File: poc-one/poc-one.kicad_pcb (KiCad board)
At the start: 2 copper layers, 275 x 200 mm, 81 parts, among them J4 Connector, USB-TYPE-C-16P, Q1 SS8550 Y2 200-350, Q2 SS8550 Y2 200-350, Q3 SS8550 Y2 200-350, Q5 SS8550 Y2 200-350, SW1 SW_Push, SW2 SW_Push, U1 RP2350_80QFN, U11 74HC595D, U13 74HC595D, U2 NCP1117-3.3_SOT223, U3 W25Q128, U4 74HC138, U9 74HC595D, Y1 ABM8-272-T3

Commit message: schematic-v2
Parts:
- added REF**: B2B Pad, TFPC:B2B Pad, F.Cu at (184.0, 81.1)
- added REF**: B2B Pad, TFPC:B2B Pad, F.Cu at (152.4, 80.5)
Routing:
- net /LED_control/LED_matrix/G2: track 14.4 -> 13.8 mm
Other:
- board outline removed

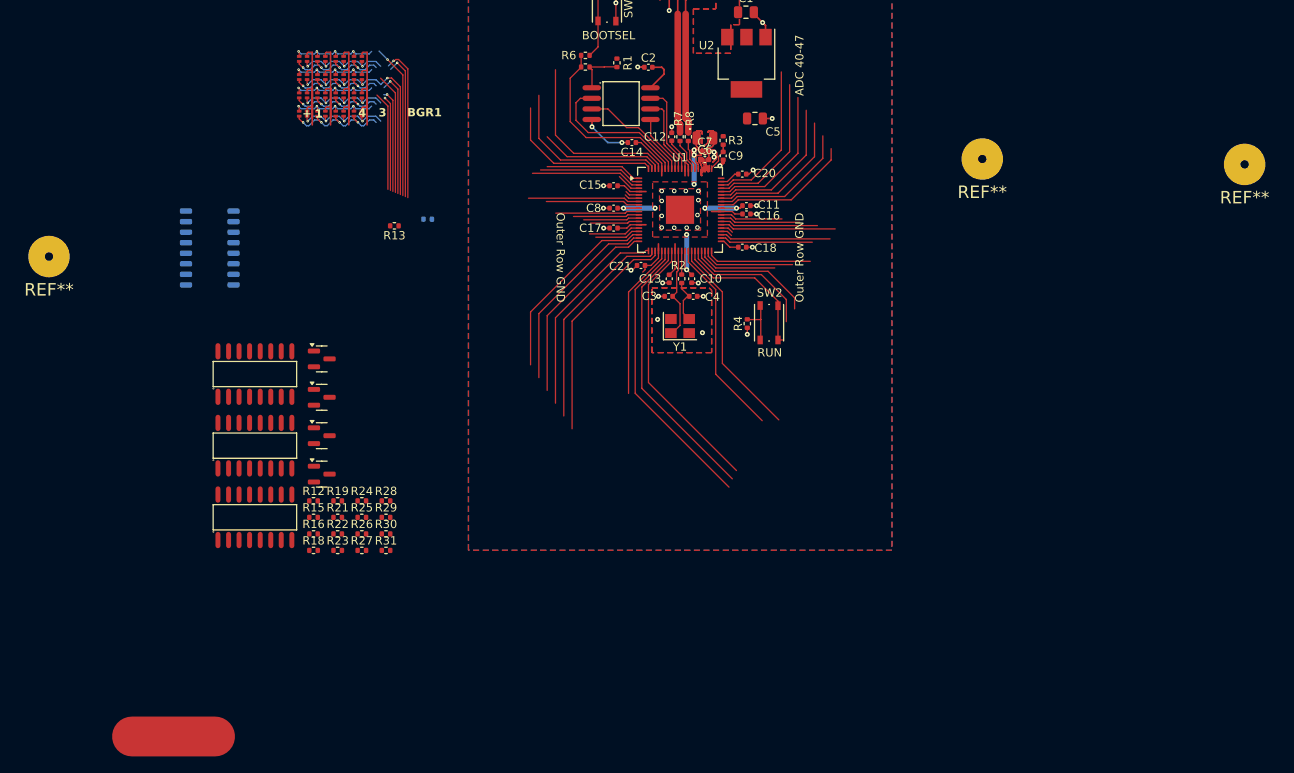
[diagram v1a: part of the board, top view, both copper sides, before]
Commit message: fixed a couple resistors, reworked footprints incl. datasheets
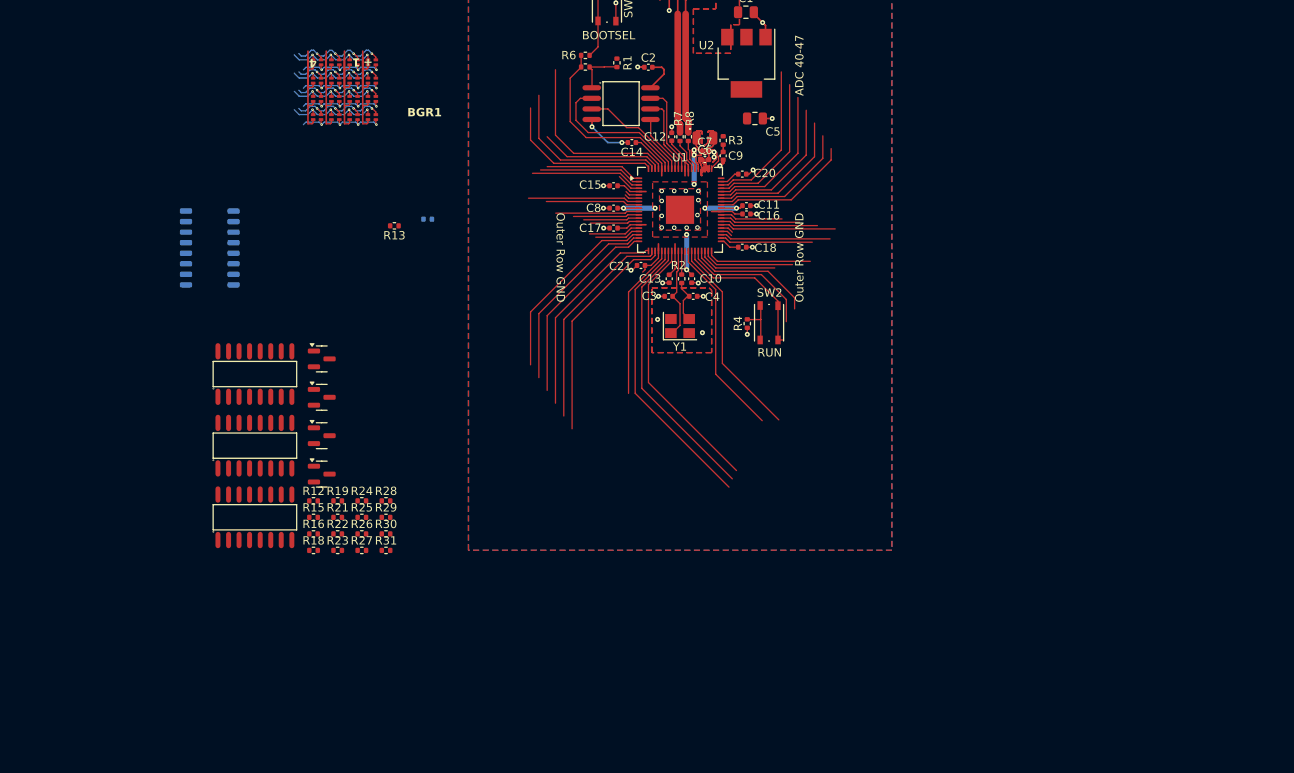
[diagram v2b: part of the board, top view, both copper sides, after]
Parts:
- removed REF** (x3): B2B Pad, TFPC:B2B Pad
- moved D1 10.9 mm to (78.9, 75.4)
- moved D13 10.3 mm to (78.9, 68.8), turned to 180 degrees
- moved D5 8.68 mm to (78.9, 73.2), turned to 180 degrees
- moved D4 8.57 mm to (72.3, 75.4), turned to 180 degrees
- moved D9 8.47 mm to (78.9, 71.0), turned to 180 degrees
- moved D2 8.02 mm to (76.7, 75.4)
- moved D16 7.90 mm to (72.3, 68.8), turned to 180 degrees
- moved D14 7.30 mm to (76.7, 68.8), turned to 180 degrees
- moved D3 7.04 mm to (74.5, 75.4), turned to 180 degrees
- moved D15 6.20 mm to (74.5, 68.8), turned to 180 degrees
- moved D8 5.57 mm to (72.3, 73.2), turned to 180 degrees
- moved D12 5.23 mm to (72.3, 71.0), turned to 180 degrees
- moved D6 4.68 mm to (76.7, 73.2), turned to 180 degrees
- moved D10 4.27 mm to (76.7, 71.0), turned to 180 degrees
- moved D7 2.67 mm to (74.5, 73.2), turned to 180 degrees
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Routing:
- net /LED_control/LED_matrix/R1: track 52.5 -> 12.7 mm, vias 7 -> 4
- net /LED_control/LED_matrix/R0: track 31.3 -> 12.7 mm, vias 5 -> 4
- net /LED_control/LED_matrix/B0: track 30.3 -> 11.7 mm, vias 5 -> 4
- net /LED_control/LED_matrix/G0: track 31.5 -> 13.8 mm, vias 5 -> 4
- net /LED_control/LED_matrix/G1: track 28.8 -> 13.8 mm, vias 5 -> 4
- net /LED_control/LED_matrix/B1: track 26.2 -> 11.7 mm
- net /LED_control/LED_matrix/B2: track 23.6 -> 11.7 mm
- net (no net): track 10.0 -> 0.00 mm
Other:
- board text removed: "3"

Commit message: poc-one routed & schematic changes
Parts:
- removed C3: 15p, Capacitor_SMD:C_0402_1005Metric
- removed the R13 at (81.6, 88.5)
- removed the R13 at (85.6, 87.7)
- removed R2: 1k, Resistor_SMD:R_0402_1005Metric
- removed U1: RP2350_80QFN, Package_DFN_QFN:QFN-80-1EP_10x10mm_P0.4mm_EP3.4x3.4mm
- removed U11, U13, U9: 74HC595D, PCM_JLCPCB:SOIC-16_L9.9-W3.9-P1.27-LS6.0-BL
- added BT1: Battery_Cell, TFPC:BH-18650-B6AA002, F.Cu at (148.4, 167.6)
- added C19: 1u, Capacitor_SMD:C_0402_1005Metric, F.Cu at (117.3, 119.7)
- added C22: 4.7u, Capacitor_SMD:C_0402_1005Metric, F.Cu at (119.6, 117.2)
- added C23: 10u, Capacitor_SMD:C_0402_1005Metric, F.Cu at (124.7, 121.7)
- added C24: 10u, Capacitor_SMD:C_0402_1005Metric, F.Cu at (127.7, 121.7)
- added C25: 10u, Capacitor_SMD:C_0402_1005Metric, F.Cu at (146.9, 119.6)
- added C26: 10u, Capacitor_SMD:C_0402_1005Metric, F.Cu at (155.7, 114.7)
- added C27: 100u, Capacitor_SMD:CP_Elec_5x5.4, F.Cu at (91.2, 206.4)
- added C35: 10u, Capacitor_SMD:C_0402_1005Metric, F.Cu at (124.0, 129.7)
- added C36: 10u, Capacitor_SMD:C_0402_1005Metric, F.Cu at (126.0, 136.4)
- added C37: 100p, Capacitor_SMD:C_0402_1005Metric, F.Cu at (124.0, 130.8)
- added C38: 100n, Capacitor_SMD:C_0402_1005Metric, F.Cu at (124.3, 137.3)
- added C39: 100n, Capacitor_SMD:C_0402_1005Metric, F.Cu at (114.3, 136.2)
- added D17: LED_RABG, TFPC:NH-B1212RGBA-HF, F.Cu at (99.7, 193.2)
- added D18: LED_RABG, TFPC:NH-B1212RGBA-HF, F.Cu at (101.9, 193.2)
- added D19: LED_RABG, TFPC:NH-B1212RGBA-HF, F.Cu at (104.1, 193.2)
- added J1: MASTER_FANOUT, Connector_PinHeader_2.54mm:PinHeader_2x10_P2.54mm_Vertical, F.Cu at (103.2, 114.1)
- added J2: SUBG_FANOUT, Connector_PinHeader_2.54mm:PinHeader_2x10_P2.54mm_Vertical, F.Cu at (83.6, 130.8)
- added J3: Connector, USB-TYPE-C-16P, PCM_JLCPCB:TYPE-C-SMD_HX-TYPE-C-16PIN, F.Cu at (110.3, 112.7)
- added J5: DEBUG, Connector_PinHeader_2.54mm:PinHeader_1x03_P2.54mm_Vertical, F.Cu at (112.8, 151.3)
- added JP1: SolderJumper_2_Bridged, Jumper:SolderJumper-2_P1.3mm_Bridged_Pad1.0x1.5mm, F.Cu at (93.8, 162.6)
- added JP10: SolderJumper_2_Bridged, Jumper:SolderJumper-2_P1.3mm_Bridged_Pad1.0x1.5mm, F.Cu at (107.2, 166.3)
- added JP11: SolderJumper_2_Bridged, Jumper:SolderJumper-2_P1.3mm_Bridged_Pad1.0x1.5mm, F.Cu at (108.4, 162.6)
- added JP12: SolderJumper_2_Bridged, Jumper:SolderJumper-2_P1.3mm_Bridged_Pad1.0x1.5mm, F.Cu at (109.8, 166.3)
- added JP13: SolderJumper_2_Bridged, Jumper:SolderJumper-2_P1.3mm_Bridged_Pad1.0x1.5mm, F.Cu at (110.9, 162.6)
- added JP14: SolderJumper_2_Bridged, Jumper:SolderJumper-2_P1.3mm_Bridged_Pad1.0x1.5mm, F.Cu at (113.0, 166.3)
- added JP15: SolderJumper_2_Bridged, Jumper:SolderJumper-2_P1.3mm_Bridged_Pad1.0x1.5mm, F.Cu at (114.1, 162.6)
- added JP16: SolderJumper_2_Bridged, Jumper:SolderJumper-2_P1.3mm_Bridged_Pad1.0x1.5mm, F.Cu at (115.5, 166.3)
- added JP17: SolderJumper_2_Bridged, Jumper:SolderJumper-2_P1.3mm_Bridged_Pad1.0x1.5mm, F.Cu at (116.7, 162.6)
- added JP18: SolderJumper_2_Bridged, Jumper:SolderJumper-2_P1.3mm_Bridged_Pad1.0x1.5mm, F.Cu at (118.9, 166.3)
- added JP19: SolderJumper_2_Bridged, Jumper:SolderJumper-2_P1.3mm_Bridged_Pad1.0x1.5mm, F.Cu at (120.0, 162.6)
- added JP2: SolderJumper_2_Bridged, Jumper:SolderJumper-2_P1.3mm_Bridged_Pad1.0x1.5mm, F.Cu at (95.2, 166.3)
- added JP20: SolderJumper_2_Bridged, Jumper:SolderJumper-2_P1.3mm_Bridged_Pad1.0x1.5mm, F.Cu at (121.5, 166.3)
- added JP21: SolderJumper_2_Bridged, Jumper:SolderJumper-2_P1.3mm_Bridged_Pad1.0x1.5mm, F.Cu at (122.6, 162.6)
- added JP3: SolderJumper_2_Bridged, Jumper:SolderJumper-2_P1.3mm_Bridged_Pad1.0x1.5mm, F.Cu at (96.3, 162.6)
- added JP4: SolderJumper_2_Bridged, Jumper:SolderJumper-2_P1.3mm_Bridged_Pad1.0x1.5mm, F.Cu at (98.8, 166.2)
- added JP5: SolderJumper_2_Bridged, Jumper:SolderJumper-2_P1.3mm_Bridged_Pad1.0x1.5mm, F.Cu at (99.9, 162.6)
- added JP6: SolderJumper_2_Bridged, Jumper:SolderJumper-2_P1.3mm_Bridged_Pad1.0x1.5mm, F.Cu at (101.3, 166.2)
- added JP7: SolderJumper_2_Bridged, Jumper:SolderJumper-2_P1.3mm_Bridged_Pad1.0x1.5mm, F.Cu at (102.5, 162.6)
- added JP8: SolderJumper_2_Bridged, Jumper:SolderJumper-2_P1.3mm_Bridged_Pad1.0x1.5mm, F.Cu at (103.8, 166.2)
- added JP9: SolderJumper_2_Bridged, Jumper:SolderJumper-2_P1.3mm_Bridged_Pad1.0x1.5mm, F.Cu at (105.0, 162.6)
- added L2: 2u2, Inductor_SMD:L_0603_1608Metric, F.Cu at (126.3, 121.2)
- added MK1: LMA2718T421-OA5-2, TFPC:LMA2718T421-OA5-2, F.Cu at (121.3, 130.7)
- added Q4: SS8550 Y2 200-350, PCM_JLCPCB:Q_SOT-23, F.Cu at (101.2, 197.6)
- added Q6: SS8550 Y2 200-350, PCM_JLCPCB:Q_SOT-23, F.Cu at (110.5, 197.6)
- added Q7: XYC-PT0805BC-L4-D, PCM_JLCPCB:D_0805, F.Cu at (121.2, 141.2)
- added R11: 5.1k, Resistor_SMD:R_0402_1005Metric, F.Cu at (107.5, 118.7)
- added R13: 2.2k, Resistor_SMD:R_0402_1005Metric, F.Cu at (117.0, 122.9)
- added R14: 100m, Resistor_SMD:R_1206_3216Metric, F.Cu at (113.8, 119.8)
- added R17: 10k, Resistor_SMD:R_0402_1005Metric, F.Cu at (121.9, 128.2)
- added R20: 1.5k, Resistor_SMD:R_0402_1005Metric, F.Cu at (120.0, 128.2)
- added R32: 130, Resistor_SMD:R_0402_1005Metric, F.Cu at (92.1, 180.9)
- added R33: 360, Resistor_SMD:R_0402_1005Metric, F.Cu at (101.1, 180.8)
- added R34: 82, Resistor_SMD:R_0402_1005Metric, F.Cu at (113.5, 181.0)
- added R35: 130, Resistor_SMD:R_0402_1005Metric, F.Cu at (93.5, 180.9)
- added R36: 360, Resistor_SMD:R_0402_1005Metric, F.Cu at (102.2, 180.8)
- added R37: 82, Resistor_SMD:R_0402_1005Metric, F.Cu at (114.8, 181.0)
- added R38: 360, Resistor_SMD:R_0402_1005Metric, F.Cu at (103.4, 180.8)
- added R39: 82, Resistor_SMD:R_0402_1005Metric, F.Cu at (116.1, 181.0)
- added R40: 360, Resistor_SMD:R_0402_1005Metric, F.Cu at (104.6, 180.8)
- added R41: 2k, Resistor_SMD:R_0402_1005Metric, F.Cu at (125.7, 130.9)
- added R42: 10k, Resistor_SMD:R_0402_1005Metric, F.Cu at (118.8, 141.2)
- added R43: 10k, Resistor_SMD:R_0402_1005Metric, F.Cu at (127.2, 136.2)
- added R44: 10k, Resistor_SMD:R_0402_1005Metric, F.Cu at (124.3, 136.3)
- added R45: 100k, Resistor_SMD:R_0402_1005Metric, F.Cu at (124.0, 131.8)
- added R46: 100, Resistor_SMD:R_0402_1005Metric, F.Cu at (121.4, 134.3)
- added SW3: BAT_SYS_PWR HY-DSIC02LS, Button_Switch_SMD:SW_DIP_SPSTx02_Slide_9.78x7.26mm_W8.61mm_P2.54mm, F.Cu at (137.8, 123.5)
- added TP1: VBUS, TestPoint:TestPoint_Pad_D1.5mm, F.Cu at (103.8, 123.0)
- added TP10: MIC_RAW, TestPoint:TestPoint_Pad_D1.5mm, F.Cu at (126.3, 128.4)
- added TP11: MIC_OUT, TestPoint:TestPoint_Pad_D1.5mm, F.Cu at (120.9, 136.9)
- added TP2: +3V8 / VSYS, TestPoint:TestPoint_Pad_D1.5mm, F.Cu at (129.7, 119.8)
- added TP3: +3V3, TestPoint:TestPoint_Pad_D1.5mm, F.Cu at (116.3, 131.6)
- added TP4: VBUS-SENSE-, TestPoint:TestPoint_Pad_D1.5mm, F.Cu at (111.2, 122.8)
- added TP5: +1V1, TestPoint:TestPoint_Pad_D1.5mm, F.Cu at (110.4, 128.9)
- added TP6: GND, TestPoint:TestPoint_Pad_D1.5mm, F.Cu at (129.7, 116.2)
- added TP7: VBAT, TestPoint:TestPoint_Pad_D1.5mm, F.Cu at (129.6, 127.1)
- added TP8: DISPLAY_SENSE+, TestPoint:TestPoint_Pad_D1.5mm, F.Cu at (82.0, 203.2)
- added TP9: DISPLAY_SENSE-, TestPoint:TestPoint_Pad_D1.5mm, F.Cu at (85.6, 203.2)
- added U10: 74HC595D, PCM_JLCPCB:SOIC-16_L9.9-W3.9-P1.27-LS6.0-BL, F.Cu at (95.3, 175.4)
- added U12: 74HC595D, PCM_JLCPCB:SOIC-16_L9.9-W3.9-P1.27-LS6.0-BL, F.Cu at (106.7, 175.6)
- added U14: 74HC595D, PCM_JLCPCB:SOIC-16_L9.9-W3.9-P1.27-LS6.0-BL, F.Cu at (118.0, 175.6)
- added U22: LMV321IDBVR, PCM_JLCPCB:SOT-23-5_L3.0-W1.7-P0.95-LS2.8-BR, F.Cu at (124.0, 134.0)
- added U6: 74HC138, Package_SO:JEITA_SOIC-16_3.9x9.9mm_P1.27mm, F.Cu at (75.0, 196.4)
- C1: value 10u -> 15p; footprint Capacitor_SMD:C_0805_2012Metric -> Capacitor_SMD:C_0402_1005Metric
- C10, C6, C9: value 4.7u -> 100n
- C2: value 100n -> 15p
- C20: value 100n -> 47n; footprint Capacitor_SMD:C_0402_1005Metric -> Capacitor_SMD:C_0603_1608Metric
- C21: value 100n -> 10u
- C4: value 15p -> 4.7u
- C5: value 10u -> 4.7u; footprint Capacitor_SMD:C_0805_2012Metric -> Capacitor_SMD:C_0402_1005Metric
- C8: value 100n -> 4.7u
- D1, D2, D3: value LED_RABG -> LED; footprint TFPC:NH-B1212RGBA-HF -> LED_SMD:LED_0603_1608Metric
- J4: value Connector, USB-TYPE-C-16P -> TOUCH_FANOUT; footprint PCM_JLCPCB:TYPE-C-SMD_HX-TYPE-C-16PIN -> Connector_PinHeader_2.54mm:PinHeader_2x08_P2.54mm_Vertical
- Q2: value SS8550 Y2 200-350 -> 2N7002
- R1: value DNF -> 0; footprint Resistor_SMD:R_0402_1005Metric -> PCM_JLCPCB:R_0603
- R10: value 0 -> 2.2k
- R12: value 82 -> 5.1k
- R15, R21: value 82 -> 10k
- R16, R22: value 360 -> 10k
- R18: value 82 -> 220
- R19: value 360 -> 5.1k
- R23: value 0 -> 10k
- R25: value 220 -> 10
- R28: value 130 -> 220
- R3: value 33 -> 1k
- R31: value 130 -> 82
- R5: value 5.1k -> 33
- R9: value 5.1k -> 330
- SW1, SW2: footprint Button_Switch_SMD:SW_Push_1P1T_NO_Vertical_Wuerth_434133025816 -> TFPC:B3U-1100PM
- U2: value NCP1117-3.3_SOT223 -> RP2354_80QFN; footprint Package_TO_SOT_SMD:SOT-223-3_TabPin2 -> Package_DFN_QFN:QFN-80-1EP_10x10mm_P0.4mm_EP3.4x3.4mm
- U3: value W25Q128 -> BQ24195LRGER; footprint PCM_JLCPCB:SOIC-8_L5.3-W5.3-P1.27-LS8.0-BL -> Package_DFN_QFN:VQFN-24-1EP_4x4mm_P0.5mm_EP2.45x2.45mm
- U4: value 74HC138 -> NCP1117-3.3_SOT223; footprint Package_SO:JEITA_SOIC-16_3.9x9.9mm_P1.27mm -> Package_TO_SOT_SMD:SOT-223-3_TabPin2; moved to F.Cu
- moved D16 127.0 mm to (97.5, 193.2), turned to 0 degrees
- moved D15 125.8 mm to (104.1, 191.1), turned to 0 degrees
- moved D14 124.8 mm to (101.9, 191.1), turned to 0 degrees
- moved D13 124.0 mm to (99.7, 191.1), turned to 0 degrees
- moved D12 122.7 mm to (97.5, 191.1), turned to 0 degrees
- moved D11 121.5 mm to (104.1, 188.8), turned to 0 degrees
- moved D10 120.5 mm to (101.9, 188.8), turned to 0 degrees
- moved D9 119.7 mm to (99.7, 188.8), turned to 0 degrees
- moved D8 118.4 mm to (97.5, 188.8), turned to 0 degrees
- moved D7 117.2 mm to (104.1, 186.7), turned to 0 degrees
- moved D6 116.2 mm to (101.9, 186.7), turned to 0 degrees
- moved D5 115.3 mm to (99.7, 186.7), turned to 0 degrees
- moved D4 114.1 mm to (97.5, 186.7), turned to 0 degrees
- moved U4 97.3 mm to (152.4, 119.7), turned to 0 degrees
- moved J4 95.3 mm to (132.1, 151.0)
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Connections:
- C1 pad 1: VBUS -> Net-(U2-XIN)
- C10 pad 1: +1V1 -> +3V3
- C11 pad 1: +1V1 -> GND
- C11 pad 2: GND -> +3.3VADC
- C2 pad 1: +3V3 -> Net-(C2-Pad1)
- C20 pad 1: +3V3 -> Net-(U3-BTST)
- C20 pad 2: GND -> Net-(C20-Pad2)
- C21 pad 1: +3V3 -> Net-(C21-Pad1)
- C4 pad 1: Net-(C4-Pad1) -> +3V3
- C5 pad 1: +3V3 -> +1V1
- C6 pad 1: +3V3 -> +1V1
- C7 pad 1: +1V1 -> Net-(U2-VREG_AVDD)
- C9 pad 1: /VREG_AVDD -> +1V1
- D1 pad 1: /LED_control/LED_matrix/R0 -> Net-(D1-K)
- D1 pad 2: /LED_control/LED_matrix/+0 -> +3V3
- D10 pad 1: /LED_control/LED_matrix/R2 -> /LED_control/LED_matrix/R1
- D10 pad 2: /LED_control/LED_matrix/+1 -> /LED_control/LED_matrix/+2
- D10 pad 3: /LED_control/LED_matrix/B2 -> /LED_control/LED_matrix/B1
- D10 pad 4: /LED_control/LED_matrix/G2 -> /LED_control/LED_matrix/G1
- D11 pad 1: /LED_control/LED_matrix/R2 -> /LED_control/LED_matrix/R1
- D11 pad 2: /LED_control/LED_matrix/+2 -> /LED_control/LED_matrix/+3
- D11 pad 3: /LED_control/LED_matrix/B2 -> /LED_control/LED_matrix/B1
- D11 pad 4: /LED_control/LED_matrix/G2 -> /LED_control/LED_matrix/G1
- D12 pad 2: /LED_control/LED_matrix/+3 -> /LED_control/LED_matrix/+0
- D13 pad 1: /LED_control/LED_matrix/R3 -> /LED_control/LED_matrix/R2
- D13 pad 2: /LED_control/LED_matrix/+0 -> /LED_control/LED_matrix/+1
- D13 pad 3: /LED_control/LED_matrix/B3 -> /LED_control/LED_matrix/B2
- D13 pad 4: /LED_control/LED_matrix/G3 -> /LED_control/LED_matrix/G2
- D14 pad 1: /LED_control/LED_matrix/R3 -> /LED_control/LED_matrix/R2
- D14 pad 2: /LED_control/LED_matrix/+1 -> /LED_control/LED_matrix/+2
- D14 pad 3: /LED_control/LED_matrix/B3 -> /LED_control/LED_matrix/B2
- D14 pad 4: /LED_control/LED_matrix/G3 -> /LED_control/LED_matrix/G2
- D15 pad 1: /LED_control/LED_matrix/R3 -> /LED_control/LED_matrix/R2
- D15 pad 2: /LED_control/LED_matrix/+2 -> /LED_control/LED_matrix/+3
- D15 pad 3: /LED_control/LED_matrix/B3 -> /LED_control/LED_matrix/B2
- D15 pad 4: /LED_control/LED_matrix/G3 -> /LED_control/LED_matrix/G2
- D16 pad 2: /LED_control/LED_matrix/+3 -> /LED_control/LED_matrix/+0
- D2 pad 1: /LED_control/LED_matrix/R0 -> Net-(D2-K)
- D2 pad 2: /LED_control/LED_matrix/+1 -> VBUS
- D3 pad 1: /LED_control/LED_matrix/R0 -> Net-(D3-K)
- D3 pad 2: /LED_control/LED_matrix/+2 -> +3V8
- D4 pad 2: /LED_control/LED_matrix/+3 -> /LED_control/LED_matrix/+0
- D5 pad 1: /LED_control/LED_matrix/R1 -> /LED_control/LED_matrix/R0
- D5 pad 2: /LED_control/LED_matrix/+0 -> /LED_control/LED_matrix/+1
- D5 pad 3: /LED_control/LED_matrix/B1 -> /LED_control/LED_matrix/B0
- D5 pad 4: /LED_control/LED_matrix/G1 -> /LED_control/LED_matrix/G0
- D6 pad 1: /LED_control/LED_matrix/R1 -> /LED_control/LED_matrix/R0
- D6 pad 2: /LED_control/LED_matrix/+1 -> /LED_control/LED_matrix/+2
- D6 pad 3: /LED_control/LED_matrix/B1 -> /LED_control/LED_matrix/B0
- D6 pad 4: /LED_control/LED_matrix/G1 -> /LED_control/LED_matrix/G0
- D7 pad 1: /LED_control/LED_matrix/R1 -> /LED_control/LED_matrix/R0
- D7 pad 2: /LED_control/LED_matrix/+2 -> /LED_control/LED_matrix/+3
- D7 pad 3: /LED_control/LED_matrix/B1 -> /LED_control/LED_matrix/B0
- D7 pad 4: /LED_control/LED_matrix/G1 -> /LED_control/LED_matrix/G0
- D8 pad 2: /LED_control/LED_matrix/+3 -> /LED_control/LED_matrix/+0
- D9 pad 1: /LED_control/LED_matrix/R2 -> /LED_control/LED_matrix/R1
- D9 pad 2: /LED_control/LED_matrix/+0 -> /LED_control/LED_matrix/+1
- D9 pad 3: /LED_control/LED_matrix/B2 -> /LED_control/LED_matrix/B1
- D9 pad 4: /LED_control/LED_matrix/G2 -> /LED_control/LED_matrix/G1
- L1 pad 2: /VREG_LX -> Net-(U2-VREG_LX)
- Q1 pad 2: +3V3 -> Net-(BT1-+)
- Q1 pad 3: /LED_control/LED_matrix/+1 -> Net-(Q1-C)
- Q2 pad 1: Net-(Q2-B) -> Net-(Q1-C)
- Q2 pad 2: +3V3 -> GND
- Q2 pad 3: /LED_control/LED_matrix/+2 -> Net-(BT1--)
- Q3 pad 2: +3V3 -> Net-(Q3-E)
- Q3 pad 3: /LED_control/LED_matrix/+3 -> /LED_control/LED_matrix/+0
- Q5 pad 2: +3V3 -> Net-(Q3-E)
- Q5 pad 3: /LED_control/LED_matrix/+0 -> /LED_control/LED_matrix/+2
- R1 pad 2: /FLASH_SS -> +3.3VADC
- R10 pad 1: /QSPI_SS -> GND
- R10 pad 2: /FLASH_SS -> Net-(D2-K)
- R12 pad 1: /LED_control/LED_matrix/B0 -> Net-(J3-CC1)
- R12 pad 2: Net-(U13-Q0) -> GND
- R15 pad 1: /LED_control/LED_matrix/B1 -> +3V8
- R15 pad 2: Net-(U13-Q1) -> Net-(U3-OTG)
- R16 pad 1: /LED_control/LED_matrix/G1 -> Net-(U3-~{CE})
- R16 pad 2: Net-(U11-Q1) -> GND
- R18 pad 1: /LED_control/LED_matrix/B2 -> Net-(U3-ILIM)
- R18 pad 2: Net-(U13-Q2) -> GND
- R19 pad 1: /LED_control/LED_matrix/G2 -> Net-(U3-REGN)
- R21 pad 1: /LED_control/LED_matrix/B3 -> Net-(Q1-C)
- R21 pad 2: Net-(U13-Q3) -> GND
- R22 pad 1: /LED_control/LED_matrix/G3 -> Net-(Q1-B)
- R22 pad 2: Net-(U11-Q3) -> Net-(BT1--)
- R23 pad 2: Net-(U4-~{E0}) -> Net-(U6-~{E0})
- R24 pad 1: Net-(U4-~{Y0}) -> Net-(U6-~{Y0})
- R24 pad 2: Net-(Q5-B) -> Net-(Q3-B)
- R25 pad 1: Net-(U4-~{Y1}) -> +3V3
- R25 pad 2: Net-(Q1-B) -> Net-(Q3-E)
- R26 pad 1: Net-(U4-~{Y2}) -> Net-(U6-~{Y1})
- R26 pad 2: Net-(Q2-B) -> Net-(Q4-B)
- R27 pad 1: Net-(U4-~{Y3}) -> Net-(U6-~{Y2})
- R27 pad 2: Net-(Q3-B) -> Net-(Q5-B)
- R28 pad 1: /LED_control/LED_matrix/R0 -> Net-(U6-~{Y3})
- R29 pad 1: /LED_control/LED_matrix/R1 -> /LED_control/LED_matrix/R0
- R3 pad 1: +3V3 -> Net-(U2-XOUT)
- R3 pad 2: /VREG_AVDD -> Net-(C2-Pad1)
- R30 pad 1: /LED_control/LED_matrix/R2 -> /LED_control/LED_matrix/R1
- R31 pad 1: /LED_control/LED_matrix/R3 -> /LED_control/LED_matrix/B0
- R5 pad 1: Net-(J4-CC1) -> +3V3
- R5 pad 2: GND -> Net-(U2-VREG_AVDD)
- R6 pad 1: /QSPI_SS -> Net-(R6-Pad1)
- R6 pad 2: /~{USB_BOOT} -> GND
- R7 pad 1: /USB_D+ -> /Battery/USB_D+
- R7 pad 2: Net-(U1-USB_DP) -> Net-(U2-USB_DP)
- R8 pad 1: /USB_D- -> /Battery/USB_D-
- R8 pad 2: Net-(U1-USB_DM) -> Net-(U2-USB_DM)
- R9 pad 1: Net-(J4-CC2) -> GND
- R9 pad 2: GND -> Net-(D1-K)
- SW1 pad 1: GND -> Net-(R6-Pad1)
- SW1 pad 2: /~{USB_BOOT} -> /BOOTSEL
- SW2 pad 2: /RUN -> /RESET
- U2 pad 1: GND -> /M-CIPO
- U2 pad 2: +3V3 -> /M-CS
- U2 pad 3: VBUS -> /Battery/SDA
- U3 pad 1: /FLASH_SS -> Net-(C19-Pad1)
- U3 pad 2: /QSPI_SD1 -> unconnected-(U3-D+-Pad2)
- U3 pad 3: /QSPI_SD2 -> unconnected-(U3-D--Pad3)
- U3 pad 4: GND -> Net-(U3-STAT)
- U3 pad 5: /QSPI_SD0 -> /Battery/SCL
- U3 pad 6: /QSPI_SCLK -> /Battery/SDA
- U3 pad 7: /QSPI_SD3 -> /Battery/INT
- U3 pad 8: +3V3 -> Net-(U3-OTG)
- U4 pad 1: /GPIO3 -> GND
- U4 pad 2: /GPIO4 -> +3V3
- U4 pad 3: /GPIO5 -> Net-(U4-VI)
- Y1 pad 1: /XIN -> Net-(U2-XIN)
- Y1 pad 3: Net-(C4-Pad1) -> Net-(C2-Pad1)
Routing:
- net Net-(BT1--): track 0.00 -> 100.9 mm, vias 0 -> 2
- net /LED_control/C_P_2: track 0.00 -> 53.3 mm, vias 0 -> 2
- net GND: track 33.1 -> 83.1 mm, vias 38 -> 72
- net /LED_control/C_P_3: track 0.00 -> 49.7 mm, vias 0 -> 2
- net /LED_control/C_P_1: track 0.00 -> 49.6 mm, vias 0 -> 2
- net Net-(U6-~{Y3}): track 0.00 -> 45.4 mm, vias 0 -> 2
- net Net-(Q3-E): track 0.00 -> 43.4 mm
- net Net-(U6-~{Y2}): track 0.00 -> 39.9 mm, vias 0 -> 2
- net /Battery/INT: track 0.00 -> 39.5 mm, vias 0 -> 4
- net /LED_control/STOP: track 0.00 -> 39.1 mm, vias 0 -> 6
- net /LED_control/~{OE}: track 0.00 -> 37.8 mm
- net /LED_control/CLK: track 0.00 -> 36.5 mm, vias 0 -> 6
- net /Battery/SCL: track 0.00 -> 35.4 mm, vias 0 -> 4
- net /GPIO25: track 34.7 -> 0.00 mm
- net Net-(U6-~{Y1}): track 0.00 -> 34.4 mm, vias 0 -> 2
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- added copper zone on F.Cu, net +3.3VADC
- added copper zone on B.Cu, net +3V8
- added copper zone on F.Cu, net +3V8
- added copper zone on F.Cu, net Net-(U2-VREG_LX)
- removed copper zone on F.Cu, net /VREG_LX
- removed copper zone on F.Cu, net VBUS
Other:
- board outline added: 95.5 x 108 mm
- rule pad_to_mask_clearance: 0.1 -> 0
- board text added: "BOOT"
- board text removed: "+"
- board text removed: "1"
- board text removed: "4"
- board text removed: "ADC 40-47"
- board text removed: "BGR1"
- board text removed: "BOOTSEL"
- board text removed: "Outer Row GND"
- board text removed: "RUN"
